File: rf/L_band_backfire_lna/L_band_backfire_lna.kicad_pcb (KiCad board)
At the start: 2 copper layers, 85.2 x 85.2 mm, 24 parts, among them J1 SMA, J2 SMA, U1 QPL9547, U2 QPL9547, X1 SAW, X2 SAW

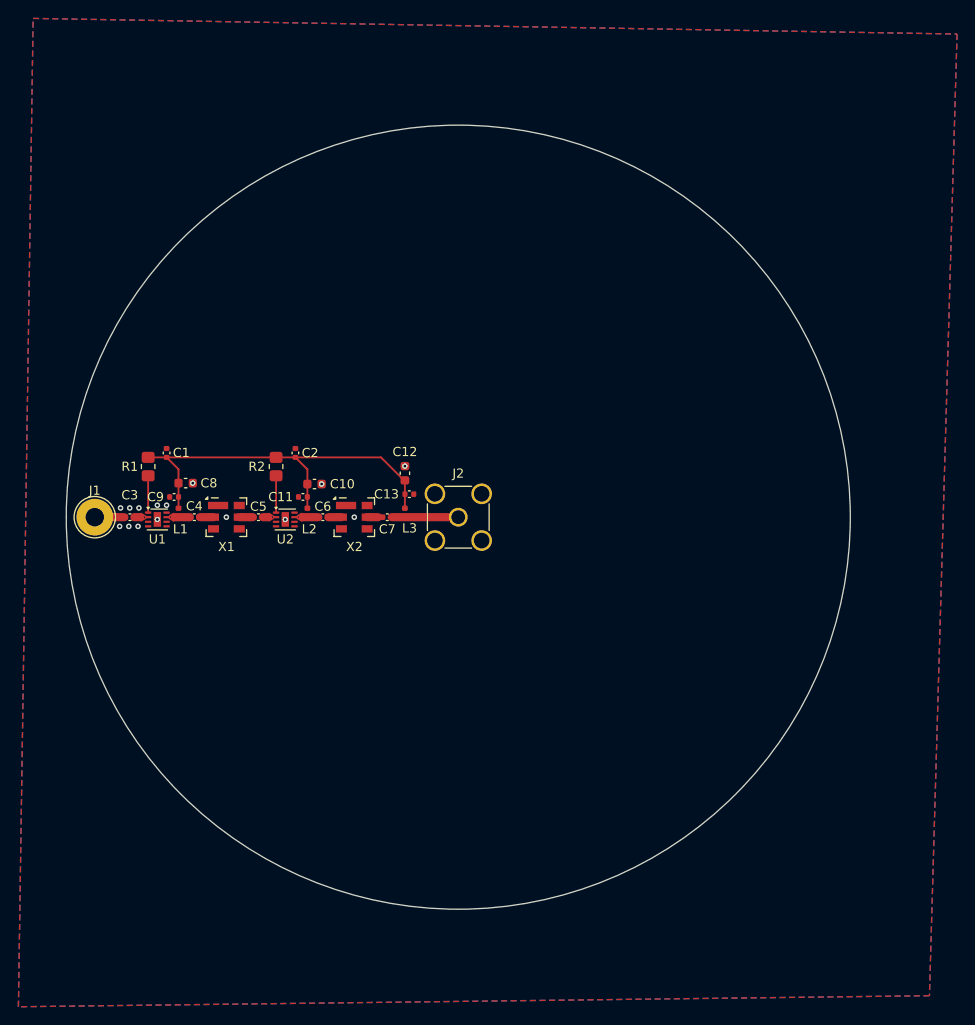
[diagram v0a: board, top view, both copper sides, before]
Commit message: Diameter =/= Radius dum dum
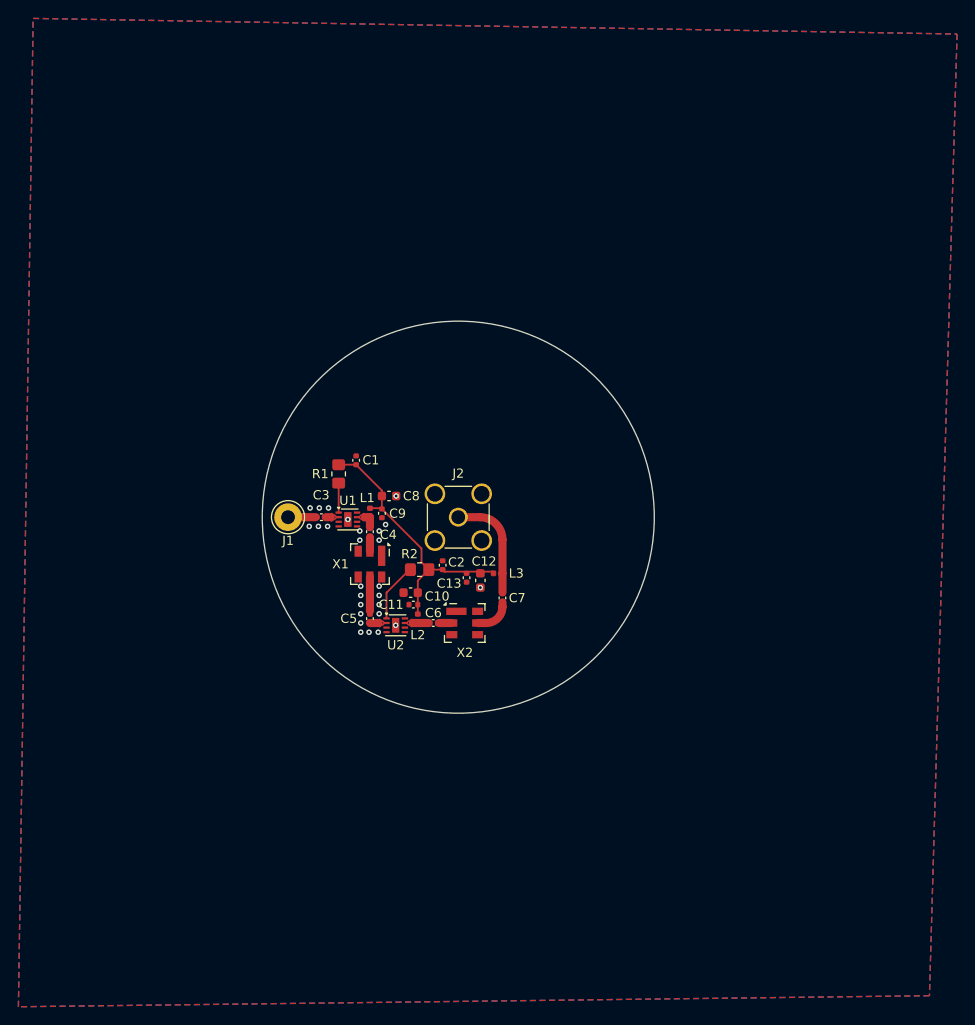
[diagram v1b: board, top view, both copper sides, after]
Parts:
- J1: footprint TestPoint:TestPoint_THTPad_D4.0mm_Drill2.0mm -> Connector_Pin:Pin_D1.3mm_L11.0mm_LooseFit
- moved C9 22.7 mm to (141.7, 99.6), turned to 90 degrees
- moved C8 22.1 mm to (142.5, 97.7)
- moved J1 21.0 mm to (131.5, 100.0)
- moved C3 20.8 mm to (135.1, 100.0)
- moved L1 20.8 mm to (140.4, 99.5)
- moved R1 20.7 mm to (137.0, 95.3)
- moved U1 20.7 mm to (138.0, 100.2)
- moved C1 20.6 mm to (138.9, 93.8)
- moved C2 20.1 mm to (148.3, 105.2)
- moved R2 19.2 mm to (145.8, 105.7), turned to 180 degrees
- moved C4 19.1 mm to (140.4, 101.6), turned to -90 degrees
- moved C11 16.8 mm to (145.1, 109.5)
- moved C6 16.6 mm to (147.3, 111.5)
- moved L2 16.6 mm to (145.6, 111.0)
- moved U2 16.6 mm to (143.2, 111.8)
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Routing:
- net VCC: track 44.1 -> 30.4 mm
- net Net-(J2-In): track 7.24 -> 11.8 mm
- net Net-(X2-OUT): track 1.20 -> 4.12 mm
- net Net-(U2-Vb): track 4.00 -> 6.44 mm
- net Net-(X1-OUT): track 1.47 -> 3.70 mm
- net Net-(U1-Vb): track 4.00 -> 3.20 mm
- net GND: vias 15 -> 27
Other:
- board size 85.2 x 85.2 mm -> 42.6 x 42.6 mm

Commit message: owo what's that :3
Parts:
- J1: footprint Connector_Pin:Pin_D1.3mm_L11.0mm_LooseFit -> Special_hole:Special Hole
- moved C2 0.96 mm to (148.3, 106.2), turned to -90 degrees
- moved L3 0.40 mm to (154.3, 105.7)
- moved C13 0.30 mm to (150.9, 106.3)
- moved C12 0.10 mm to (152.4, 106.8)
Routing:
- net GND: vias 27 -> 90
